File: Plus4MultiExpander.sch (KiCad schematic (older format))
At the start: 17 parts, among them CN1 EDGE_CONN, CN2 C16_NEWSTYLE_EXP_PORT_1, CN3 C16_NEWSTYLE_EXP_PORT_2, CN4 C16_NEWSTYLE_EXP_PORT_3, U1 74HCT245, U2 74HCT245, U3 74HCT08

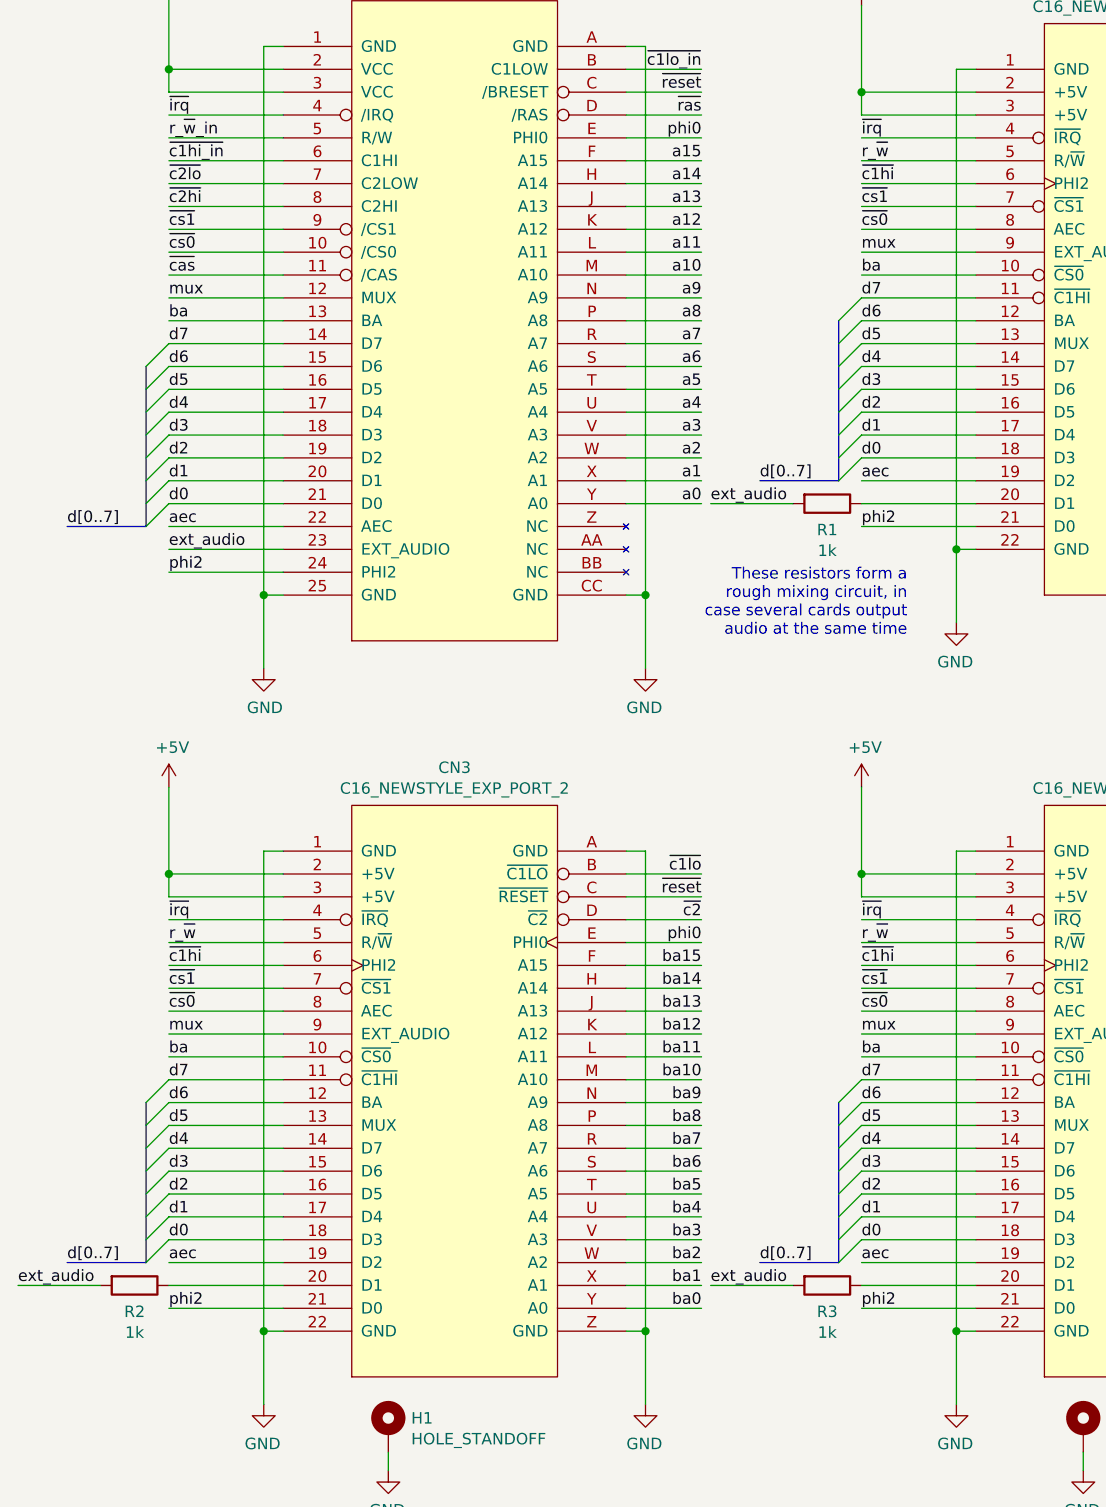
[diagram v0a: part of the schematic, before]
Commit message: New pin mapping
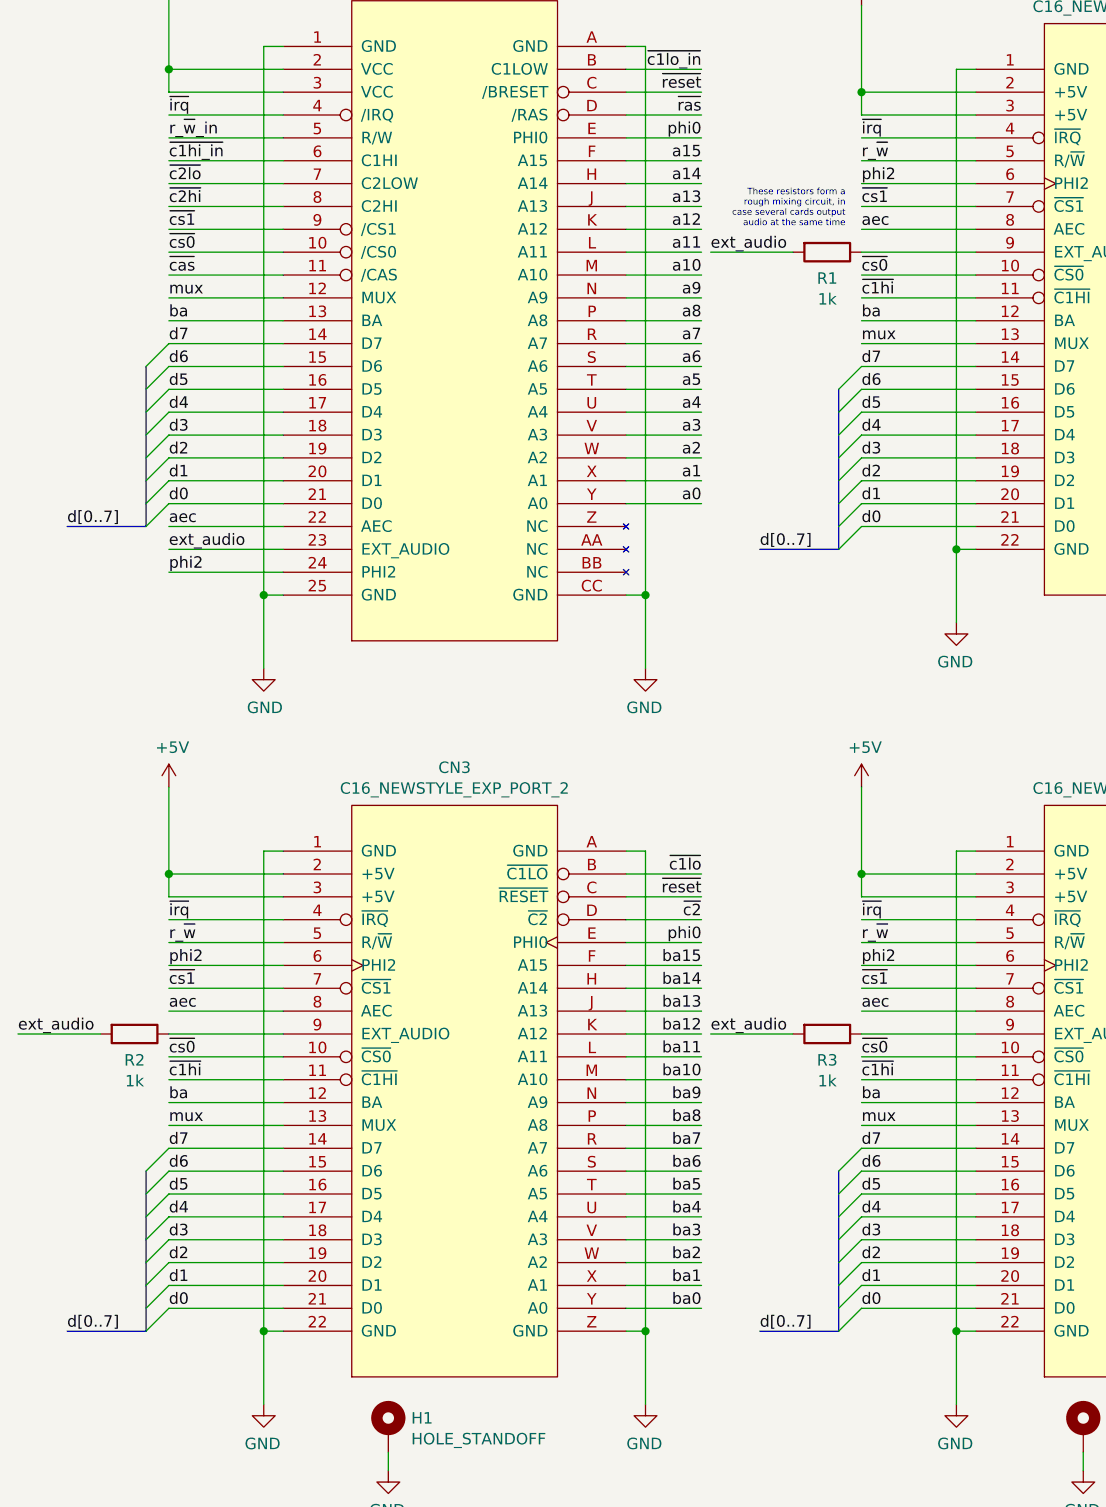
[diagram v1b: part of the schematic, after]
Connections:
- net aec: now also CN2.8 (AEC), CN3.8 (AEC), CN4.8 (AEC); no longer CN2.19 (D2), CN3.19 (D2), CN4.19 (D2)
- net ba: now also CN2.12 (BA), CN3.12 (BA), CN4.12 (BA); no longer CN2.10 (~CS0), CN3.10 (~CS0), CN4.10 (~CS0)
- net d0: now also CN2.21 (D0), CN3.21 (D0), CN4.21 (D0); no longer CN2.18 (D3), CN3.18 (D3), CN4.18 (D3)
- net d1: now also CN2.20 (D1), CN3.20 (D1), CN4.20 (D1); no longer CN2.17 (D4), CN3.17 (D4), CN4.17 (D4)
- net d2: now also CN2.19 (D2), CN3.19 (D2), CN4.19 (D2); no longer CN2.16 (D5), CN3.16 (D5), CN4.16 (D5)
- net d3: now also CN2.18 (D3), CN3.18 (D3), CN4.18 (D3); no longer CN2.15 (D6), CN3.15 (D6), CN4.15 (D6)
- net d4: now also CN2.17 (D4), CN3.17 (D4), CN4.17 (D4); no longer CN2.14 (D7), CN3.14 (D7), CN4.14 (D7)
- net d5: now also CN2.16 (D5), CN3.16 (D5), CN4.16 (D5); no longer CN2.13 (MUX), CN3.13 (MUX), CN4.13 (MUX)
- net d6: now also CN2.15 (D6), CN3.15 (D6), CN4.15 (D6); no longer CN2.12 (BA), CN3.12 (BA), CN4.12 (BA)
- net d7: now also CN2.14 (D7), CN3.14 (D7), CN4.14 (D7); no longer CN2.11 (~C1HI), CN3.11 (~C1HI), CN4.11 (~C1HI)
- net mux: now also CN2.13 (MUX), CN3.13 (MUX), CN4.13 (MUX); no longer CN2.9 (EXT_AUDIO), CN3.9 (EXT_AUDIO), CN4.9 (EXT_AUDIO)
- net phi2: now also CN2.6 (PHI2), CN3.6 (PHI2), CN4.6 (PHI2); no longer CN2.21 (D0), CN3.21 (D0), CN4.21 (D0)
- net ~c1hi: now also CN2.11 (~C1HI), CN3.11 (~C1HI), CN4.11 (~C1HI); no longer CN2.6 (PHI2), CN3.6 (PHI2), CN4.6 (PHI2)
- net ~cs0: now also CN2.10 (~CS0), CN3.10 (~CS0), CN4.10 (~CS0); no longer CN2.8 (AEC), CN3.8 (AEC), CN4.8 (AEC)
- net at R3.1: now also CN4.9 (EXT_AUDIO); no longer CN4.20 (D1)
- net at R2.1: now also CN3.9 (EXT_AUDIO); no longer CN3.20 (D1)
- net at R1.1: now also CN2.9 (EXT_AUDIO); no longer CN2.20 (D1)
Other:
- moved on the sheet: R1

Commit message: Refinements
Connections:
- net r_~w: now also U3.11; no longer U3.6
- net r_~w~_in: now also U3.12, U3.13; no longer U3.4, U3.5
- net ~c1hi: now also U3.6; no longer U3.11
- net ~c1hi_in: now also U3.4, U3.5; no longer U3.12, U3.13
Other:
- moved on the sheet: U3B, U3D
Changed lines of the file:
@@
 L 74xx:74LS08 U3
 U 2 1 65AB918C
-P 10225 5760
-F 0 "U3" H 10225 6085 50  0000 C CNN
-F 1 "74HCT08" H 10225 5994 50  0000 C CNN
-F 2 "Package_DIP:DIP-14_W7.62mm_Socket_LongPads" H 10225 5760 50  0001 C CNN
-F 3 "http://www.ti.com/lit/gpn/sn74LS08" H 10225 5760 50  0001 C CNN
-	2    10225 5760
+P 10225 5195
+F 0 "U3" H 10225 5520 50  0000 C CNN
+F 1 "74HCT08" H 10225 5429 50  0000 C CNN
+F 2 "Package_DIP:DIP-14_W7.62mm_Socket_LongPads" H 10225 5195 50  0001 C CNN
+F 3 "http://www.ti.com/lit/gpn/sn74LS08" H 10225 5195 50  0001 C CNN
+	2    10225 5195
 	1    0    0    -1
 $EndComp
@@
 L 74xx:74LS08 U3
 U 4 1 65ABD51B
-P 10225 5195
-F 0 "U3" H 10225 5520 50  0000 C CNN
-F 1 "74HCT08" H 10225 5429 50  0000 C CNN
-F 2 "Package_DIP:DIP-14_W7.62mm_Socket_LongPads" H 10225 5195 50  0001 C CNN
-F 3 "http://www.ti.com/lit/gpn/sn74LS08" H 10225 5195 50  0001 C CNN
-	4    10225 5195
+P 10225 5760
+F 0 "U3" H 10225 6085 50  0000 C CNN
+F 1 "74HCT08" H 10225 5994 50  0000 C CNN
+F 2 "Package_DIP:DIP-14_W7.62mm_Socket_LongPads" H 10225 5760 50  0001 C CNN
+F 3 "http://www.ti.com/lit/gpn/sn74LS08" H 10225 5760 50  0001 C CNN
+	4    10225 5760
 	1    0    0    -1
 $EndComp

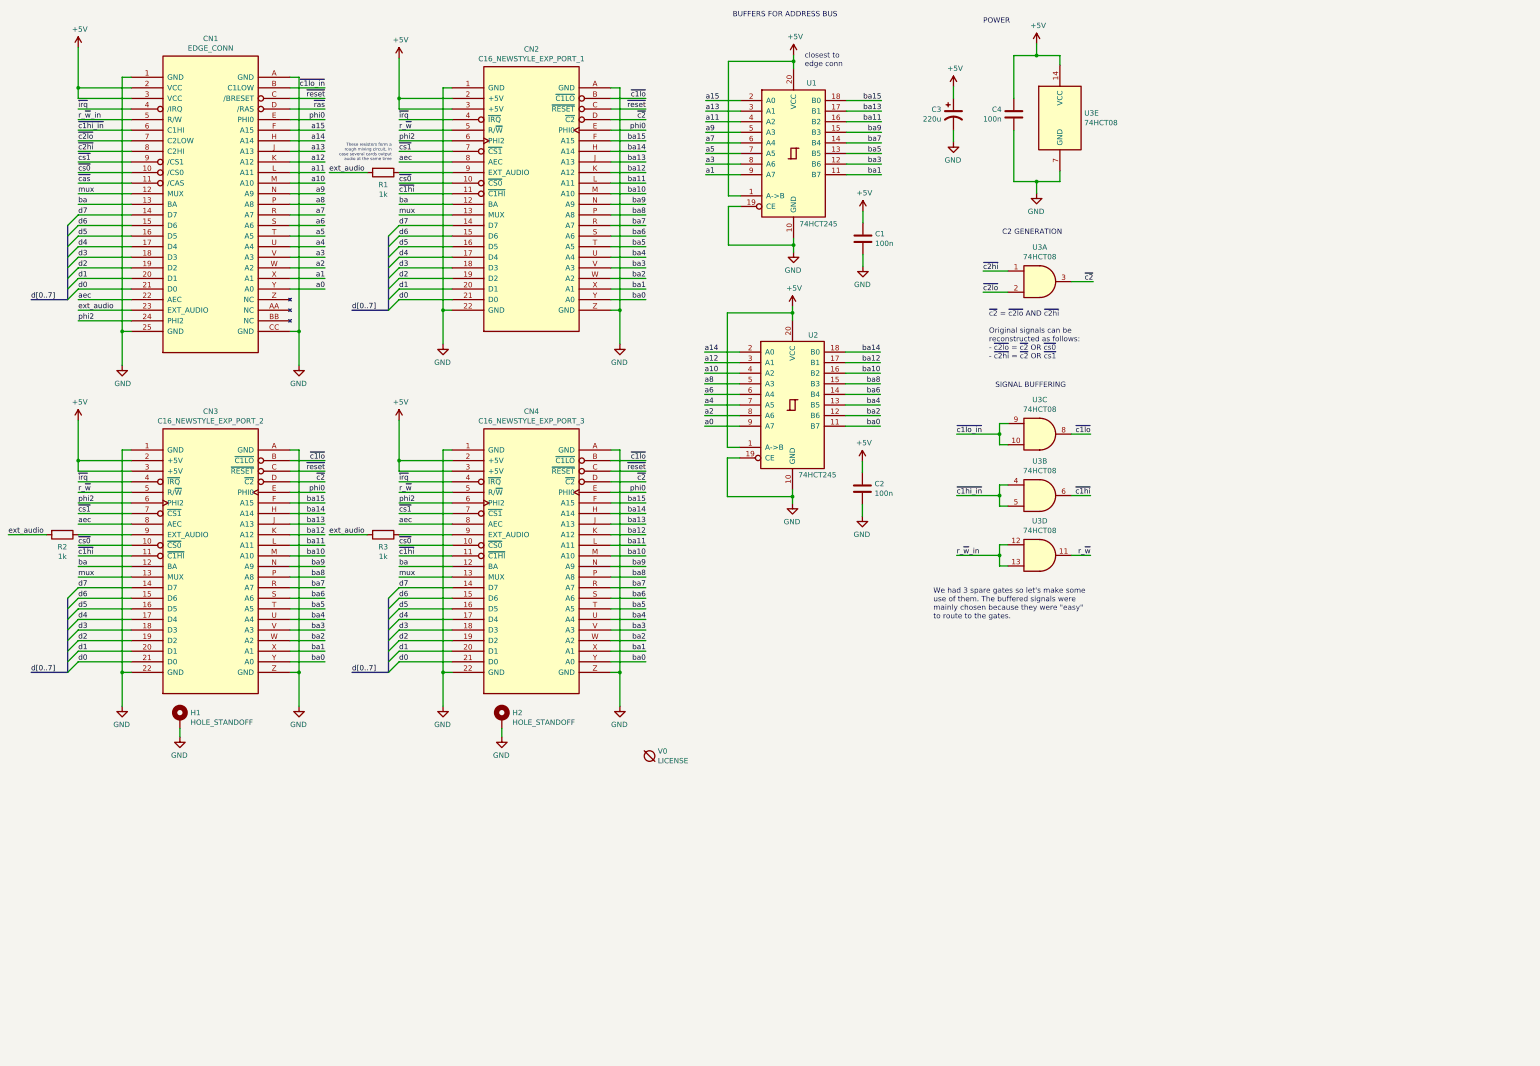
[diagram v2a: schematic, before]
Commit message: Active mixer prototype
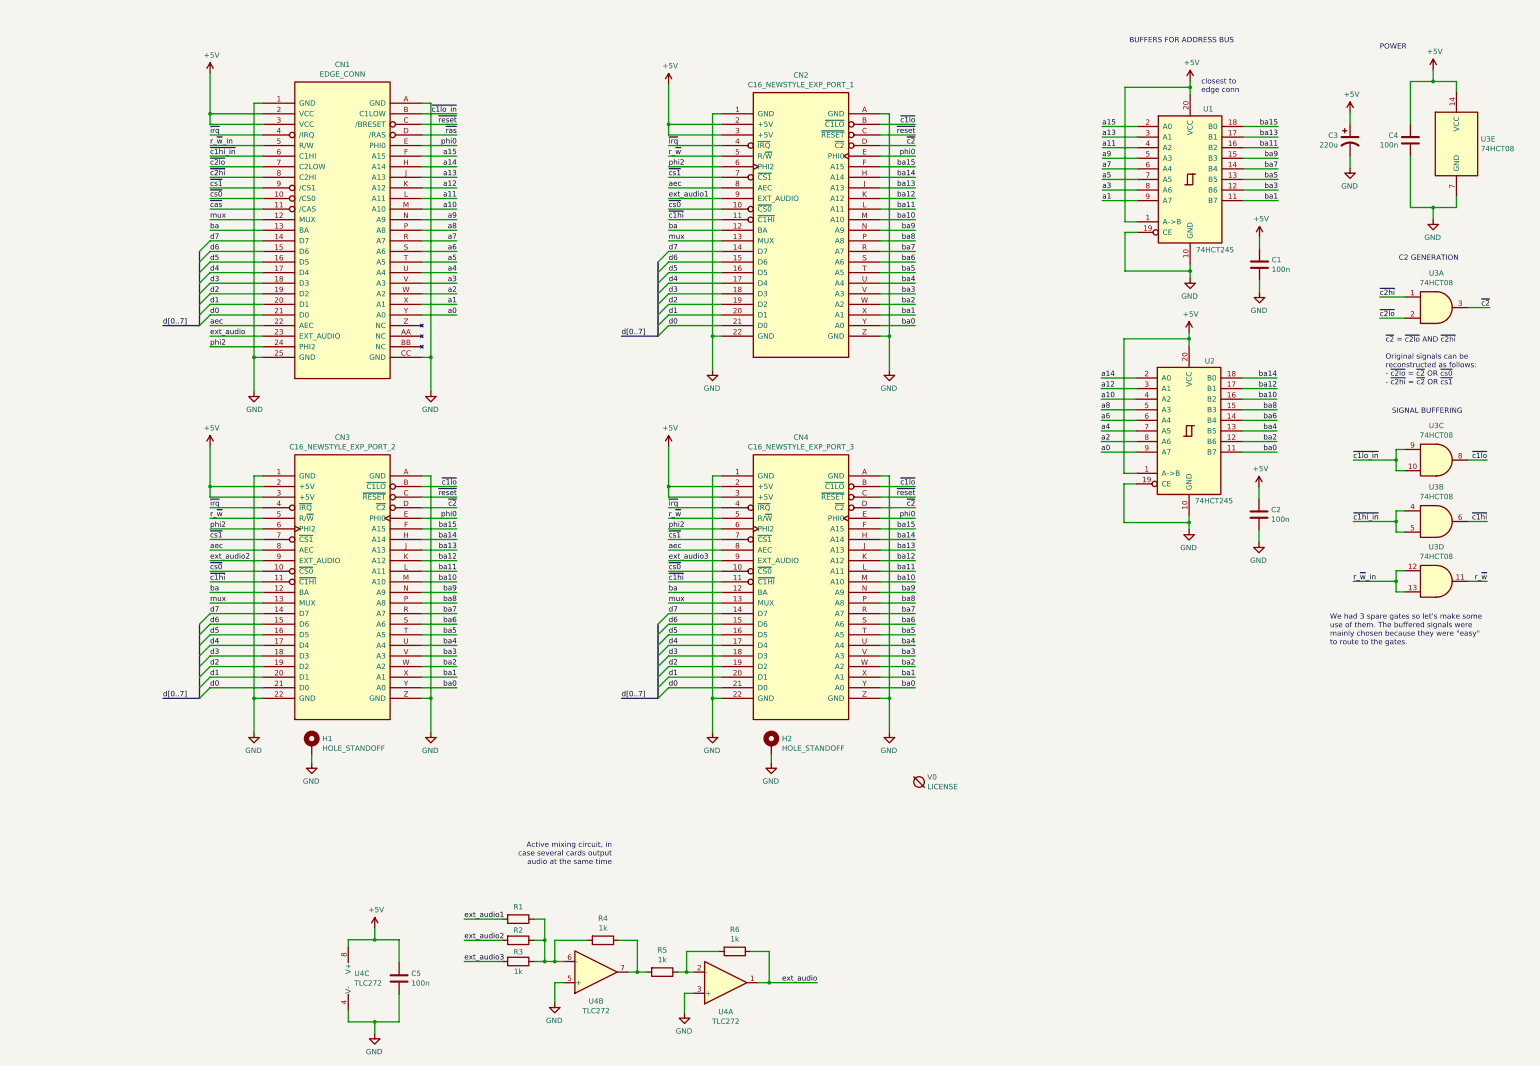
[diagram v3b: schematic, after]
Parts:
- added C5: 100n, Capacitor_THT:C_Disc_D7.0mm_W2.5mm_P5.00mm, symbol Device:C
- added R4, R5, R6: 1k, Resistor_THT:R_Axial_DIN0204_L3.6mm_D1.6mm_P7.62mm_Horizontal, symbol Device:R
- added U4: TLC272, Package_DIP:DIP-8_W7.62mm_Socket_LongPads, symbol Amplifier_Operational:TLC272
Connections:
- net +5V: now also C5.1, U4.8 (V+)
- net GND: now also C5.2, U4.3 (+), U4.4 (V-), U4.5 (+)
- net ext_audio: now also R6.1, U4.1; no longer R1.2, R2.2, R3.2
- net at R3.1: now also R1.1, R2.1, R4.2, U4.6 (-); no longer CN4.9 (EXT_AUDIO)
- net ext_audio2: now reaches CN3.9 (EXT_AUDIO)
- net ext_audio2: now also R2.2; no longer R2.1
- net ext_audio1: now reaches CN2.9 (EXT_AUDIO)
- net ext_audio1: now also R1.2; no longer R1.1
- new net: R5.1, R6.2, U4.2 (-)
- new net: R4.1, R5.2, U4.7
- new net ext_audio3: CN4.9 (EXT_AUDIO), R3.2
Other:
- note added: "Active mixing circuit, in\ncase several cards output\naudio at the same time"
- note removed: "These resistors form a\nrough mixing circuit, in\ncase several cards output\naudio at the same time"
- moved on the sheet: C1, C2, C3, C4, CN1, CN2, CN3, CN4, H1, H2, R1, R2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
